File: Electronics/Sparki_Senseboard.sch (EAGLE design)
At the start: 21 parts

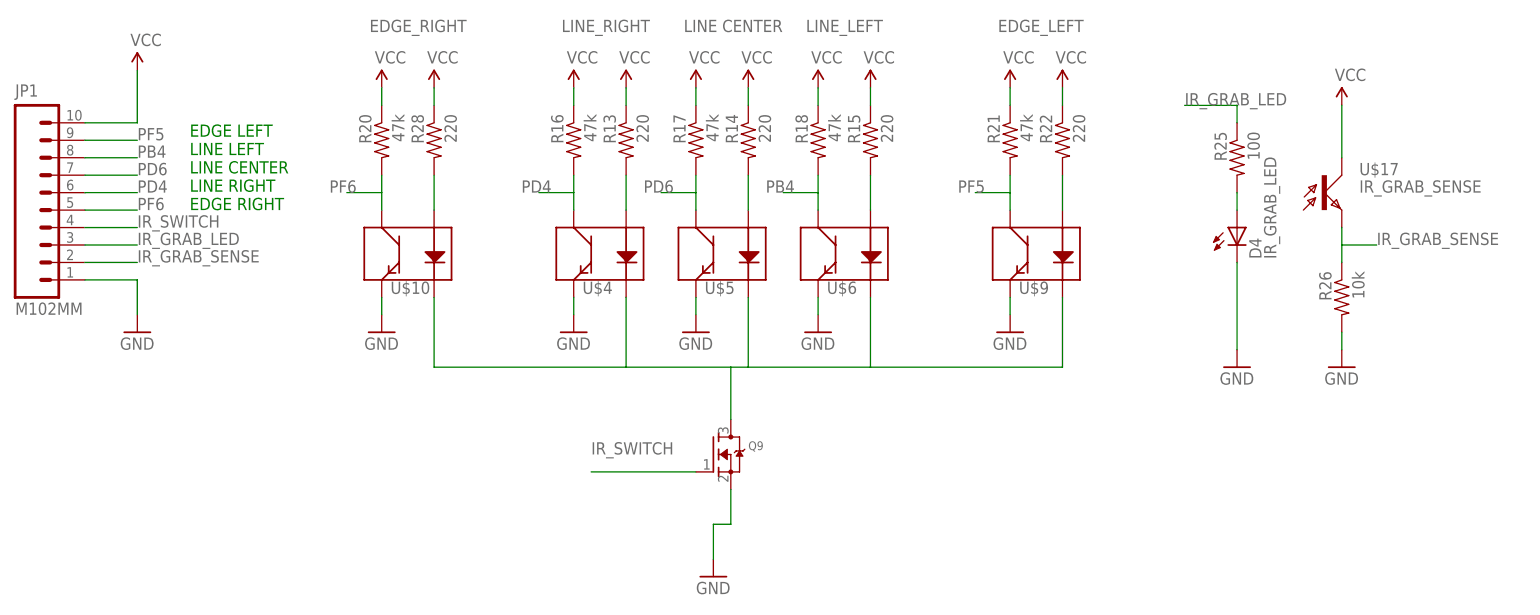
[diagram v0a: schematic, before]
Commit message: Updated connectors, sensor multiplexing
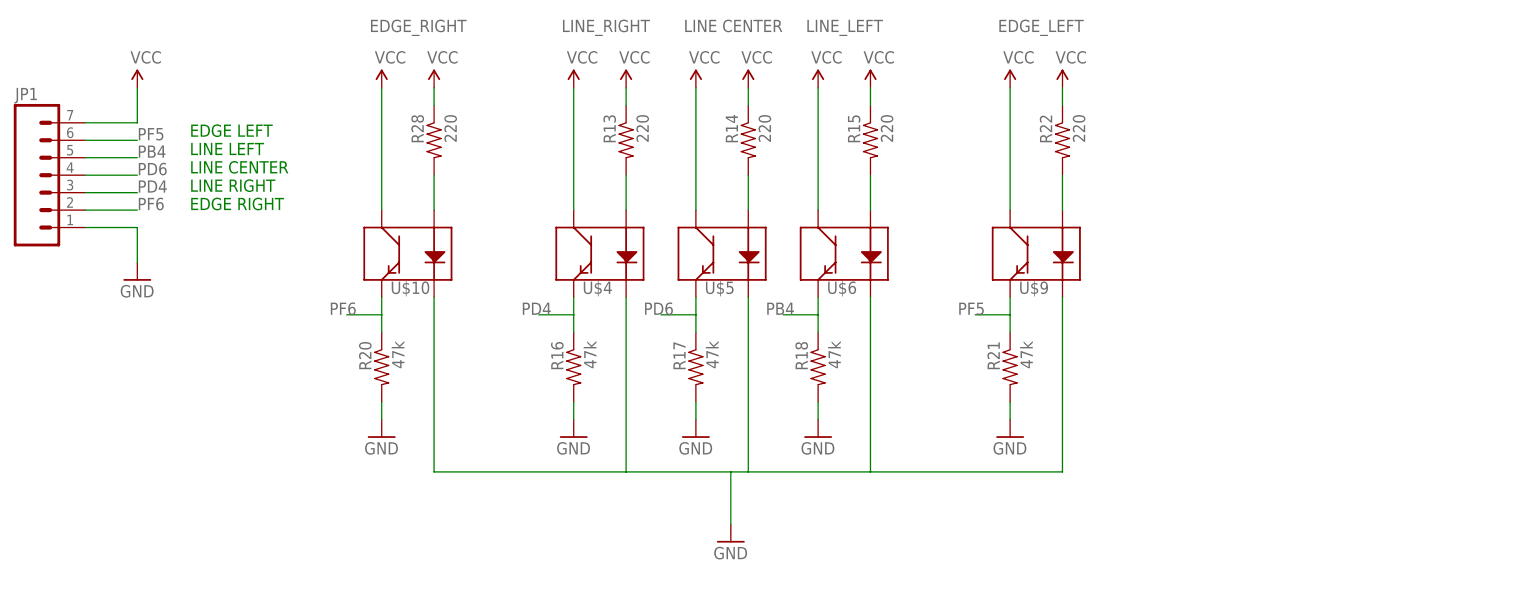
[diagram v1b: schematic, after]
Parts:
- removed D4: IR_GRAB_LED, arcbotics:LED-FKIT-1206
- removed Q9: (no value), adafruit:MOSFET-NREFLOW
- removed R25: 100, SparkFun-Passives:RESISTOR0603-RES
- removed R26: 10k, SparkFun-Passives:RESISTOR0603-RES
- removed U$17: IR_GRAB_SENSE, arcbotics:PHOTOTRANSISTOR1206
- JP1: value M102MM -> (none); device arcbotics:M102MM -> SparkFun-Connectors:M07
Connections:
- removed net IR_GRAB_LED: JP1.3, R25.1
- removed net IR_GRAB_SENSE: JP1.2, R26.1, U$17.E
- removed net IR_SWITCH: JP1.4, Q9.G
- removed net N$25: Q9.D, U$10.K, U$4.K, U$5.K, U$6.K, U$9.K
- removed net N$33: D4.A, R25.2
- net GND: now also R16.2, R17.2, R18.2, R20.2, R21.2, U$10.K, U$4.K, U$5.K, U$6.K, U$9.K; no longer D4.C, Q9.S, R26.2, U$10.E, U$4.E, U$5.E, U$6.E, U$9.E
- net PB4: now also JP1.5, R18.1, U$6.E; no longer JP1.8, R18.2, U$6.C
- net PD4: now also JP1.3, R16.1, U$4.E; no longer JP1.6, R16.2, U$4.C
- net PD6: now also JP1.4, R17.1, U$5.E; no longer JP1.7, R17.2, U$5.C
- net PF5: now also JP1.6, R21.1, U$9.E; no longer JP1.9, R21.2, U$9.C
- net PF6: now also JP1.2, R20.1, U$10.E; no longer JP1.5, R20.2, U$10.C
- net VCC: now also JP1.7, U$10.C, U$4.C, U$5.C, U$6.C, U$9.C; no longer JP1.10, R16.1, R17.1, R18.1, R20.1, R21.1, U$17.C
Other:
- moved on the sheet: R16, R17, R18, R20, R21
